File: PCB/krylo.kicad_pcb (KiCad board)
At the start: 2 copper layers, 135.3 x 87.6 mm, 52 parts, among them SW1 Switch, SW10 Switch, SW11 Switch, SW12 Switch, SW13 Switch, SW14 Switch, SW15 Switch, SW16 Switch, SW2 Switch, SW3 Switch, SW4 Switch, SW5 Switch, SW6 Switch, SW7 Switch, SW8 Switch, SW9 Switch, U1 nice_nano

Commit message: Mount points repositioned. Edge cuts revisioned, starting to position the Molex_connector
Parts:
- removed H5: Mount, krylo:SMT_M2
- moved JP1 42.3 mm to (105.8, 105.8), turned to 90 degrees
- moved JP4 42.3 mm to (105.8, 105.8), turned to 90 degrees
- moved JP2 39.9 mm to (108.3, 105.8), turned to 90 degrees
- moved JP3 39.9 mm to (108.3, 105.8), turned to 90 degrees
- moved H3 39.4 mm to (89.7, 116.7)
- moved BT1 25.6 mm to (128.3, 111.8), turned to 180 degrees
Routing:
- net Net-(SW_PWR1-B_back): track 55.9 -> 15.9 mm, vias 3 -> 2
- net col_D: track 183.4 -> 194.1 mm
- net col_E: track 206.8 -> 217.3 mm
- net row_C: track 98.2 -> 99.4 mm
- net GND: vias 5 -> 4
- removed copper zone on B.Cu, net GND
- removed copper zone on F.Cu, net GND
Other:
- outline, holes or cut-outs redrawn

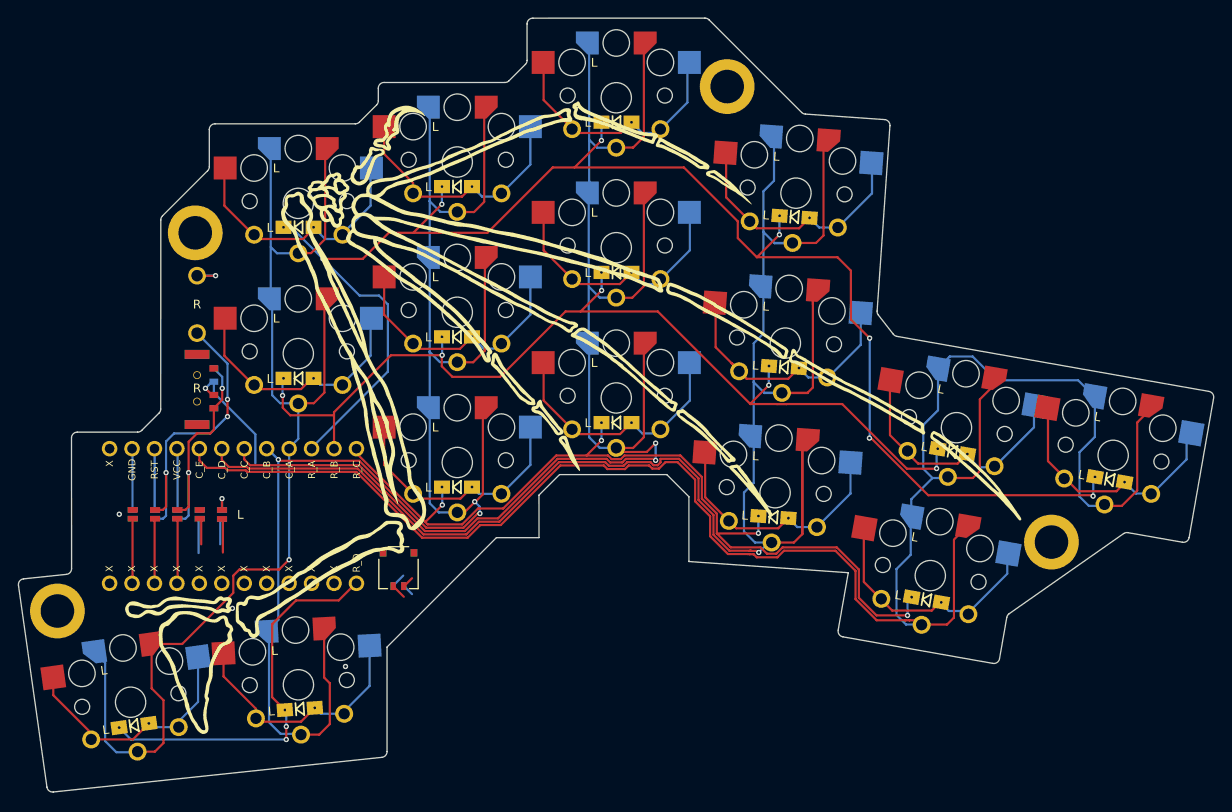
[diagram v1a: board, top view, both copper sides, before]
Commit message: Molex footprint side hint, 3D model placement correction. Zone fill
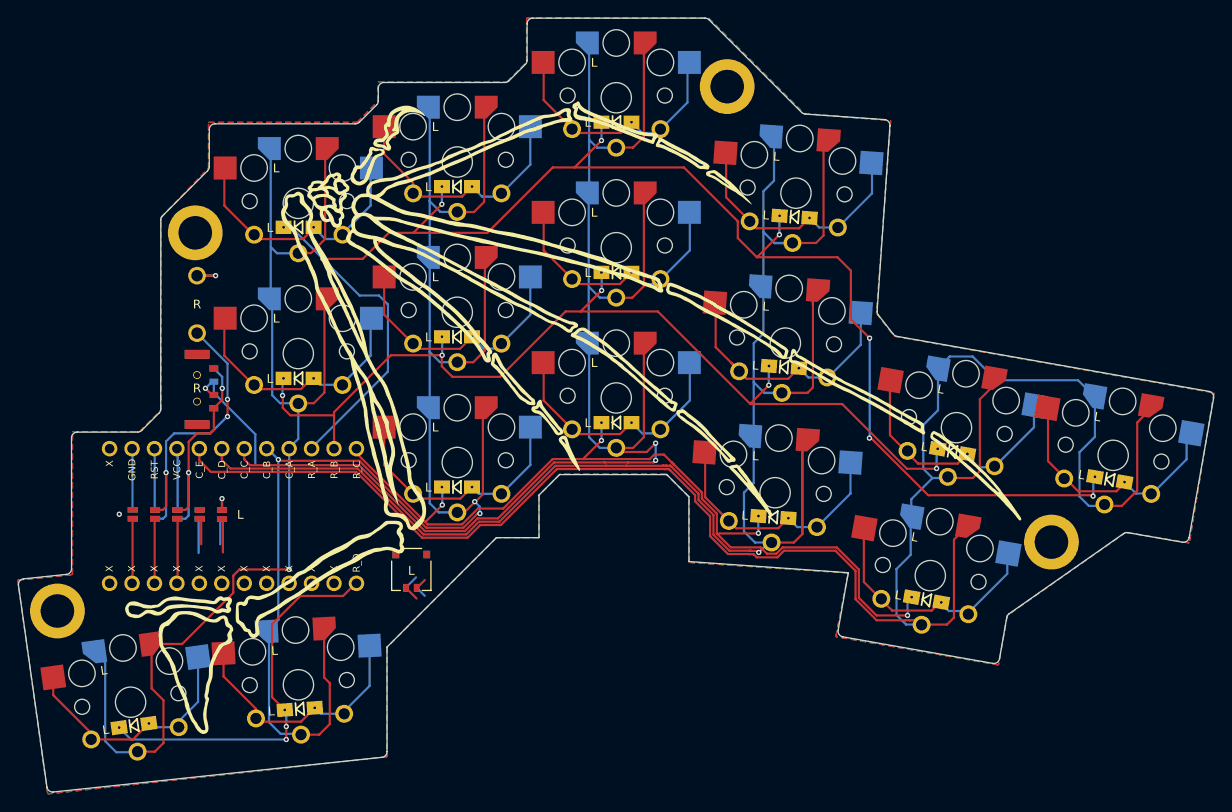
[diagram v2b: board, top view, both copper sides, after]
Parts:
- moved BT1 1.46 mm to (129.8, 112.0)
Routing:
- net col_D: track 194.1 -> 191.6 mm
- net col_E: track 217.3 -> 215.0 mm
- net row_C: track 99.4 -> 98.7 mm
- net col_A: track 130.2 -> 130.8 mm
- net GND: vias 4 -> 2
- added copper zone on B.Cu, net GND
- added copper zone on F.Cu, net GND

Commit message: Power connector double-side use routing configuration done
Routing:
- net /PAD1: track 8.21 -> 34.7 mm, vias 0 -> 1
- net /PAD2: track 10.8 -> 31.2 mm, vias 0 -> 1
- net Net-(SW_PWR1-B_back): track 15.9 -> 21.7 mm
- net RESET: track 34.0 -> 33.5 mm
- net +BATT: track 26.1 -> 25.6 mm
- net GND: vias 2 -> 1

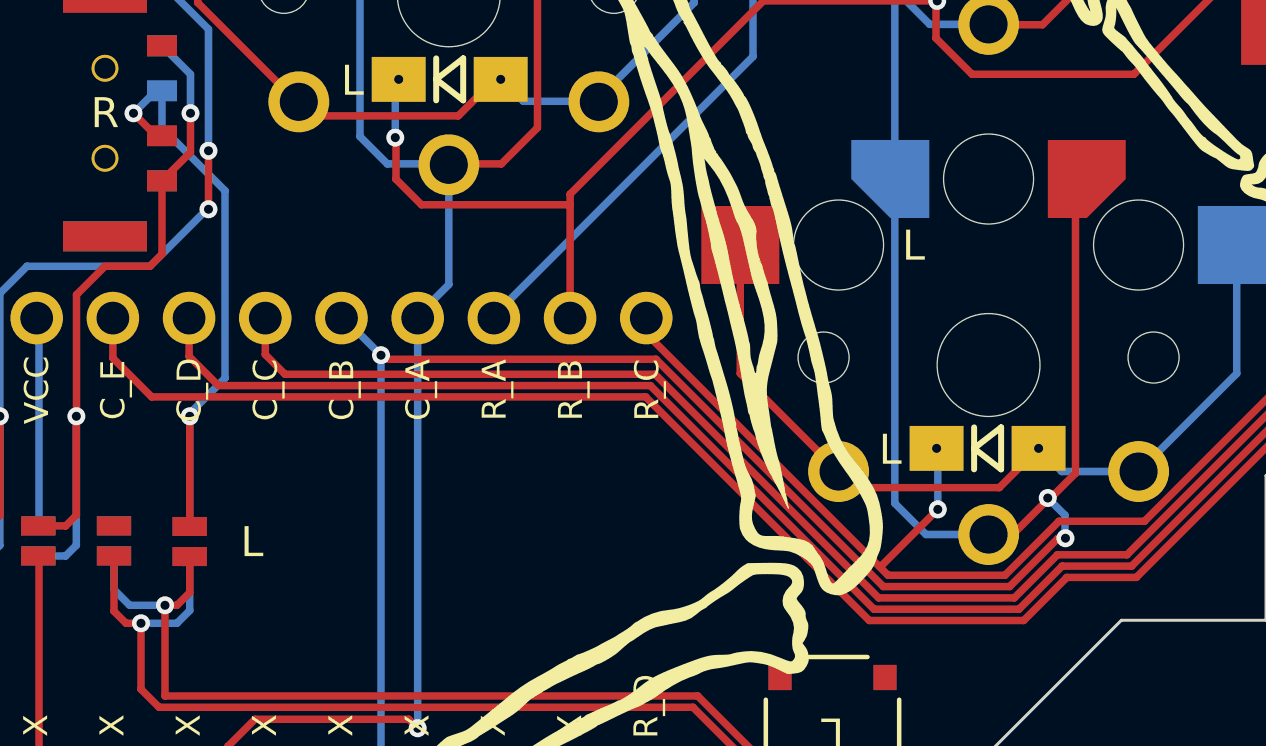
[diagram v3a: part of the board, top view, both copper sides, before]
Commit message: Updates pull, refill, tracks clean up
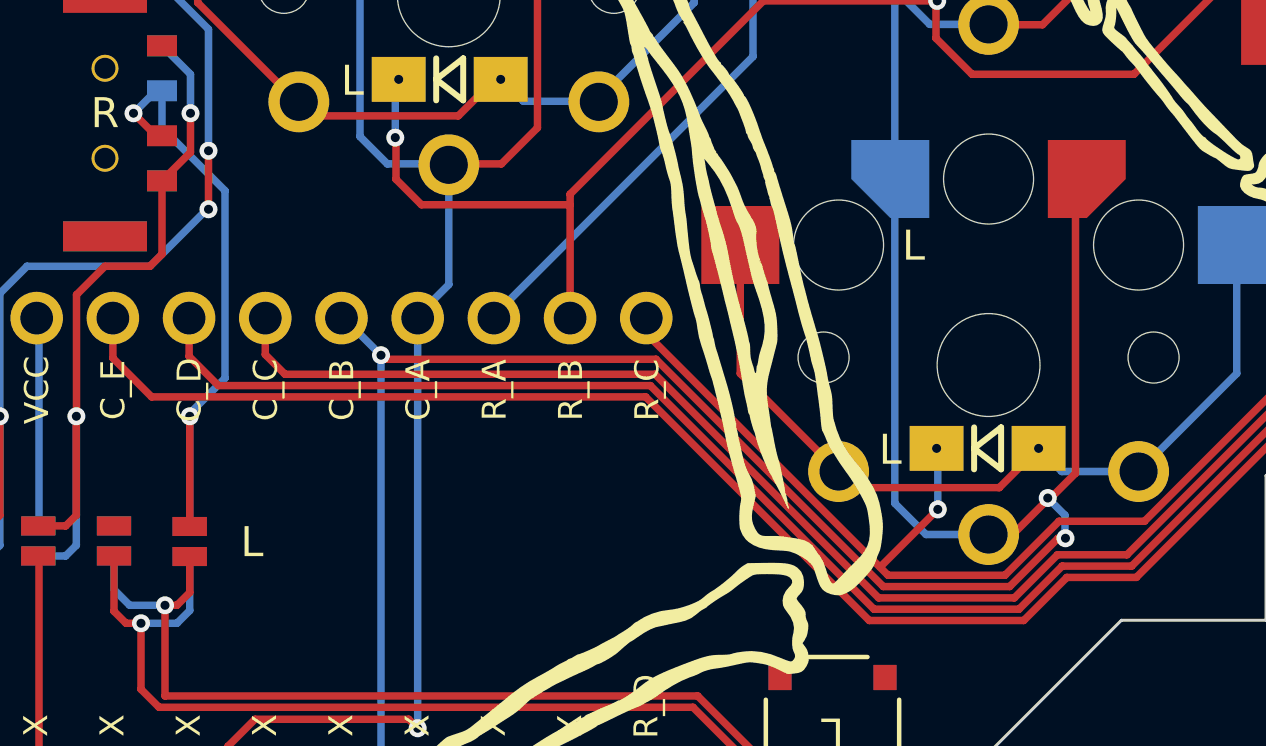
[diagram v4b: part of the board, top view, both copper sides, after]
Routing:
- net col_B: track 175.4 -> 174.3 mm
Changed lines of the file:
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@@
-	)
-	(segment
-		(start 137.85 94.075)
-		(end 138.075479 93.849521)
-		(width 0.25)
-		(layer "F.Cu")
-		(net "col_B")
 	)
 	(segment
@@
 		(net "col_B")
 	)
-	(segment
-		(start 135.75 105.55)
-		(end 134.95 105.55)
-		(width 0.25)
-		(layer "F.Cu")
-		(net "col_B")
-	)
 	(via
 		(at 114.7 99.564866)
@@
 		(width 0.25)
 		(layer "B.Cu")
-		(net "/PAD1")
-	)
-	(segment
-		(start 108.325 106.275)
-		(end 108.125 106.475)
-		(width 0.25)
-		(layer "B.Cu")
